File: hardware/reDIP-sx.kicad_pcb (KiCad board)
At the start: 6 copper layers, 17.8 x 40.6 mm, 134 parts, among them J1 DX07S016JA3, J10 Conn_01x01, J2 Conn_01x01, J3 Conn_01x01, J4 Conn_01x01, J5 Conn_01x06, J6 Conn_01x06, J7 Conn_01x10, J8 Conn_01x10, J9 Conn_01x01, Q1 PEMH4, Q2 PDTA143ZMB, U1 NCP163AFCT120T2G, U10 CBTD3306GT, U11 SN74CBTD16211DGVR, U2 NCP167AFCT330T2G, U3 FSA221UMX, U4 SGTL5000XNLA3, U5 ESP32-PICO-V3-02, U6 CP2102N-A02-GQFN24, U7 FSA8049UCX, U8 ICE40UP5K-SG48I, U9 APS6404L-3SQR-SN

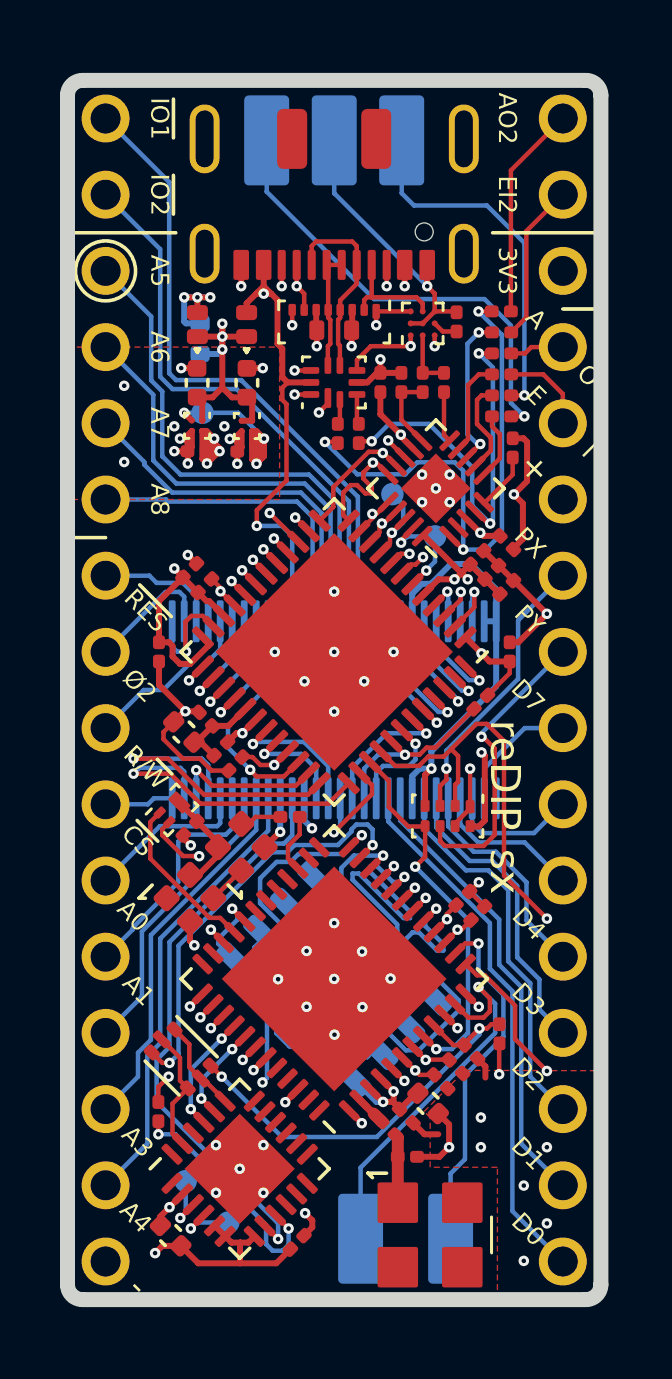
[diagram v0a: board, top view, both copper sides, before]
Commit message: Usability and manufacturability improvements
* Swapped pins for 3V3 and AO2
* Replaced 0.35mm pitch BGA LDOs with larger pitch parts, improved layout
* Removed IO2 pullup
* Added solder pad for RGB LED strip
* Increased solder mask clearance
* Updated silk screen
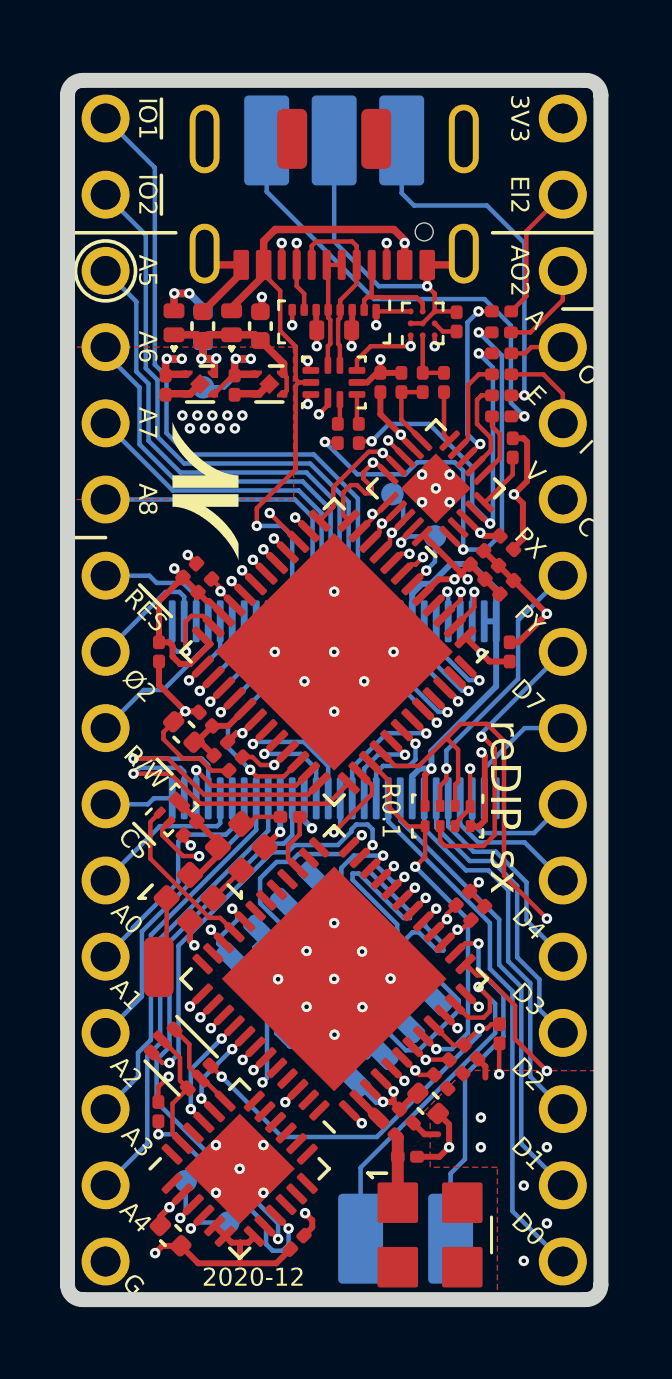
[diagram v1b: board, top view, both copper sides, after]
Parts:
- removed R12: 2.2k, Resistor_SMD:R_0201_0603Metric
- removed the SolderMask Opening D0.2mm at (105.3, 105.6)
- removed the SolderMask Opening D0.2mm at (104.1, 105.6)
- removed the SolderMask Opening D0.2mm at (103.6, 105.6)
- removed the SolderMask Opening D0.2mm at (102.5, 105.6)
- removed the SolderMask Opening D0.2mm at (105.0, 106.4)
- removed the SolderMask Opening D0.2mm at (102.3, 105.2)
- removed the SolderMask Opening D0.4mm at (105.3, 105.6)
- removed the SolderMask Opening D0.4mm at (102.7, 106.4)
- removed the SolderMask Opening D0.4mm at (102.3, 106.0)
- removed the SolderMask Opening D0.4mm at (102.3, 105.2)
- removed the SolderMask Opening D0.4mm at (104.1, 105.6)
- removed the SolderMask Opening D0.4mm at (103.6, 105.6)
- removed the SolderMask Opening D0.4mm at (102.5, 105.6)
- removed the SolderMask Opening D0.4mm at (103.8, 106.0)
- removed the SolderMask Opening D0.4mm at (104.0, 105.2)
- removed the SolderMask Opening D0.4mm at (105.0, 106.4)
- removed the SolderMask Opening D0.4mm at (104.4, 106.4)
- removed the SolderMask Opening D0.4mm at (103.4, 106.4)
- added J2: Conn_01x01, reDIP:SolderWirePad_1x01_SMD_1x2mm, F.Cu at (101.8, 123.2)
- added SolderMask Opening D0.2mm: SolderMask_Opening_D0.2mm, reDIP:SolderMask_Opening_D0.2mm, F.Cu at (103.3, 105.2)
- added SolderMask Opening D0.2mm: SolderMask_Opening_D0.2mm, reDIP:SolderMask_Opening_D0.2mm, F.Cu at (103.6, 104.8)
- added SolderMask Opening D0.2mm: SolderMask_Opening_D0.2mm, reDIP:SolderMask_Opening_D0.2mm, F.Cu at (103.1, 104.8)
- added SolderMask Opening D0.4mm: SolderMask_Opening_D0.4mm, reDIP:SolderMask_Opening_D0.4mm, B.Cu at (103.3, 105.2)
- added SolderMask Opening D0.4mm: SolderMask_Opening_D0.4mm, reDIP:SolderMask_Opening_D0.4mm, B.Cu at (103.6, 104.8)
- added SolderMask Opening D0.4mm: SolderMask_Opening_D0.4mm, reDIP:SolderMask_Opening_D0.4mm, B.Cu at (103.1, 104.8)
- added SolderMask Opening D0.4mm: SolderMask_Opening_D0.4mm, reDIP:SolderMask_Opening_D0.4mm, B.Cu at (104.1, 104.8)
- added SolderMask Opening D0.4mm: SolderMask_Opening_D0.4mm, reDIP:SolderMask_Opening_D0.4mm, B.Cu at (103.8, 105.2)
- added SolderMask Opening D0.4mm: SolderMask_Opening_D0.4mm, reDIP:SolderMask_Opening_D0.4mm, B.Cu at (104.3, 105.2)
- added SolderMask Opening D0.4mm: SolderMask_Opening_D0.4mm, reDIP:SolderMask_Opening_D0.4mm, B.Cu at (104.6, 104.8)
- added SolderMask Opening D0.4mm: SolderMask_Opening_D0.4mm, reDIP:SolderMask_Opening_D0.4mm, B.Cu at (102.6, 104.8)
- added SolderMask Opening D0.4mm: SolderMask_Opening_D0.4mm, reDIP:SolderMask_Opening_D0.4mm, B.Cu at (102.8, 105.2)
- added svg2mod: G***, reDIP:Nimrod-N, F.Cu at (103.3, 107.3)
- U1: value NCP163AFCT120T2G -> NCP163AMX120TBG; footprint ONSemi:WLCSP-4_0.64x0.64mm_Layout2x2_P0.35mm -> ONSemi:CASE711AJ_1.0x1.0mm_P0.65mm
- U2: value NCP167AFCT330T2G -> NCP167AMX330TBG; footprint ONSemi:WLCSP-4_0.64x0.64mm_Layout2x2_P0.35mm -> ONSemi:CASE711AJ_1.0x1.0mm_P0.65mm
- moved C4 2.44 mm to (102.0, 103.8), turned to 270 degrees
- moved C2 2.25 mm to (104.3, 103.8), turned to 270 degrees
- moved SolderMask Opening D0.2mm 1.99 mm to (104.6, 104.8)
- moved C1 1.94 mm to (105.2, 101.8)
- moved C3 1.90 mm to (103.2, 101.8)
- moved SolderMask Opening D0.2mm 1.61 mm to (102.6, 104.8)
- moved U1 1.59 mm to (105.5, 103.8), turned to 0 degrees
- moved U2 1.39 mm to (103.2, 103.8), turned to 0 degrees
- moved SolderMask Opening D0.2mm 1.22 mm to (104.1, 104.8)
- moved SolderMask Opening D0.2mm 1.18 mm to (104.3, 105.2)
- moved SolderMask Opening D0.2mm 0.92 mm to (102.8, 105.2)
- moved TP1 0.85 mm to (103.2, 103.9)
- moved D2 0.78 mm to (102.3, 101.7)
- moved C11 0.70 mm to (113.2, 101.3)
- moved C20 0.70 mm to (113.2, 102.0)
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- renumbered J9 to J10, J10 to J11, J2 to J3, J3 to J4, J4 to J5, J5 to J6, J6 to J7, J7 to J8, J8 to J9
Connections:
- D5 pad 1: (no net) -> /LED_DO
- J7 pad 1: /AUDIO_OUT_2 -> +3V3
- J7 pad 3: +3V3 -> /AUDIO_OUT_2
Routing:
- net +5V: track 45.5 -> 39.7 mm, vias 5 -> 4
- net +3V3: track 72.3 -> 66.9 mm, vias 22 -> 21
- net /AUDIO_OUT_2: track 7.15 -> 3.15 mm
- net VBUS: track 24.9 -> 28.3 mm, vias 4 -> 3
- net /D-: track 35.6 -> 32.5 mm
- net /ICE_~IO2~: track 6.12 -> 3.18 mm
- net /CC2: track 34.6 -> 37.5 mm
- net GND: track 64.9 -> 67.7 mm, vias 59 -> 57
- net /D+: track 36.1 -> 33.5 mm
- net /LED_DO: track 0.00 -> 2.40 mm
- net /A_SEL: track 53.6 -> 51.8 mm
- net /CC1: track 40.4 -> 42.2 mm
- net /Vcc: track 28.0 -> 26.5 mm, vias 3 -> 2
- net /~IO2~: track 19.0 -> 20.2 mm
- net /~IO1~: track 21.8 -> 22.9 mm
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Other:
- rule pad_to_mask_clearance: 0.025 -> 0.05
- board text added: "2020-12"
- board text added: "28"
- board text added: "A2"
- board text added: "C"
- board text added: "G"
- board text added: "L"
- board text added: "R"
- board text added: "R0.1"
- board text added: "V"
- board text removed: "+"
- board text removed: "-"
- board text removed: "27"
- board text removed: "4"
- board text removed: "5"
- board text removed: "LNL"
- board text removed: "LNR"

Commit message: A few small improvements
* Added SPI SCLK source termination for iCE40UP5K
* Changed R11 to 100Ω
* Changed C27 to 0.1µF
* Replaced a few capacitors with more readily available parts
* Added datasheet URLs for all parts
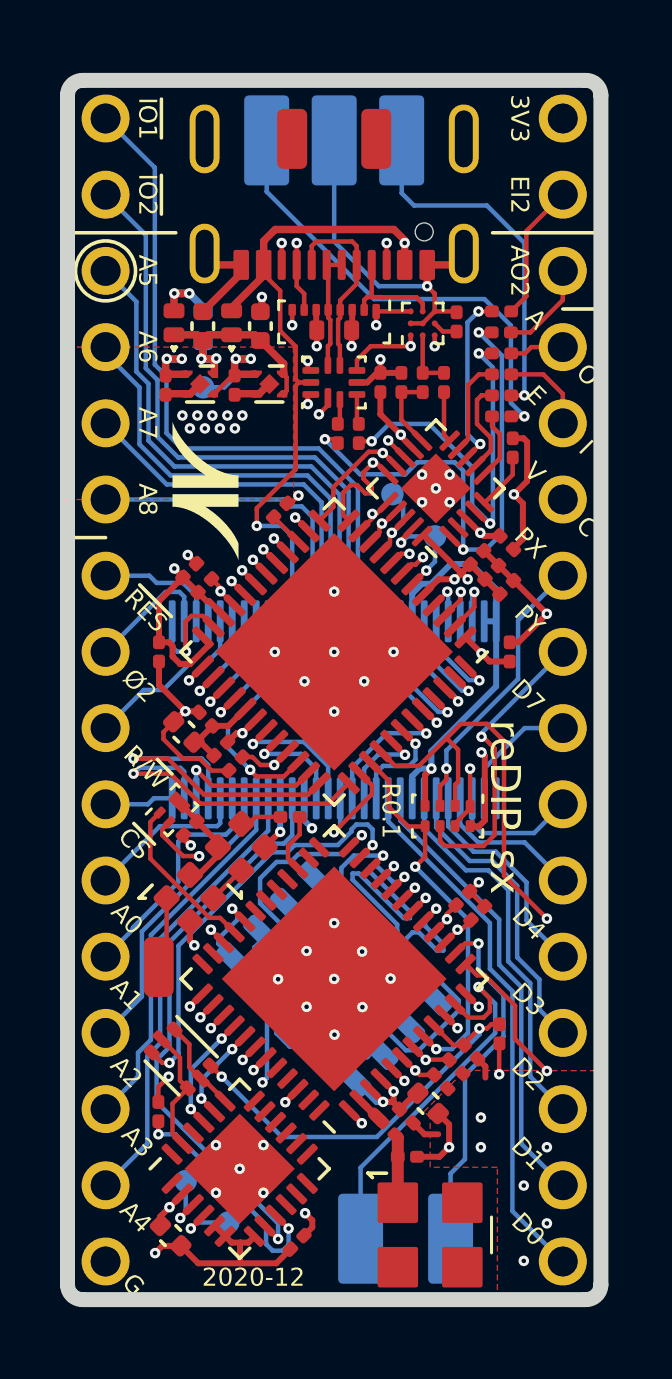
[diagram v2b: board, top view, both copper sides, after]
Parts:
- added R12: 22, Resistor_SMD:R_0201_0603Metric, F.Cu at (105.8, 108.0)
- C27: value 1uF -> 0.1uF
- R11: value 330 -> 100
- renumbered J3 to J2, J4 to J3, J5 to J4, J6 to J5, J7 to J6, J8 to J7, J9 to J8, J2 to J9
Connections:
- U8 pad 15: /SPI_SCLK -> Net-(R12-Pad1)
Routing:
- net /SPI_SCLK: track 32.4 -> 30.4 mm
- net Net-(R12-Pad1): track 0.00 -> 1.17 mm

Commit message: Usability and manufacturability improvements
* Increased minimum via size (good luck on increasing it further!)
* Corrected footprint rotation for D3 (IPC-7351)
* Removed split in stencil apertures for pin-in-paste
* Changed to shorter pin USB-C receptacle, yielding improved hole
  fill for partial pin penetration soldering
* Adjustments to fab and silk screen layers
* Added alternative ESP32 APLL configuration example to schematic
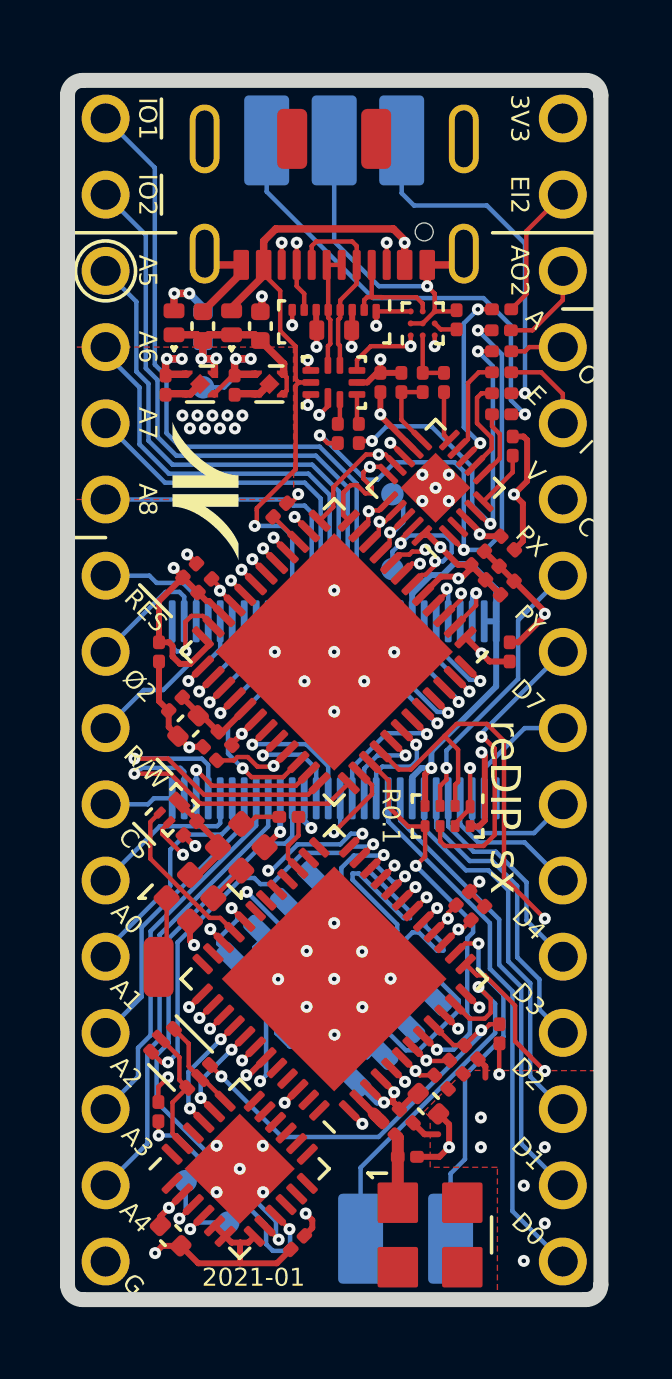
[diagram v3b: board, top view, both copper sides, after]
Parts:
- removed SolderMask Opening D0.4mm: SolderMask_Opening_D0.4mm, reDIP:SolderMask_Opening_D0.4mm (x9)
- added SolderMask D0.45mm: SolderMask_D0.45mm, reDIP:SolderMask_D0.45mm, B.Cu at (103.3, 105.2)
- added SolderMask D0.45mm: SolderMask_D0.45mm, reDIP:SolderMask_D0.45mm, B.Cu at (103.6, 104.8)
- added SolderMask D0.45mm: SolderMask_D0.45mm, reDIP:SolderMask_D0.45mm, B.Cu at (103.1, 104.8)
- added SolderMask D0.45mm: SolderMask_D0.45mm, reDIP:SolderMask_D0.45mm, B.Cu at (104.1, 104.8)
- added SolderMask D0.45mm: SolderMask_D0.45mm, reDIP:SolderMask_D0.45mm, B.Cu at (103.8, 105.2)
- added SolderMask D0.45mm: SolderMask_D0.45mm, reDIP:SolderMask_D0.45mm, B.Cu at (104.3, 105.2)
- added SolderMask D0.45mm: SolderMask_D0.45mm, reDIP:SolderMask_D0.45mm, B.Cu at (104.6, 104.8)
- added SolderMask D0.45mm: SolderMask_D0.45mm, reDIP:SolderMask_D0.45mm, B.Cu at (102.6, 104.8)
- added SolderMask D0.45mm: SolderMask_D0.45mm, reDIP:SolderMask_D0.45mm, B.Cu at (102.8, 105.2)
- J1: footprint JAE:USB_C_Receptacle_JAE_DX07S016JA3_PinInPaste -> JAE:USB_C_Receptacle_JAE_DX07S016JA1
- SolderMask D0.25mm: renamed from SolderMask Opening D0.2mm; value SolderMask_Opening_D0.2mm -> SolderMask_D0.25mm; footprint reDIP:SolderMask_Opening_D0.2mm -> reDIP:SolderMask_D0.25mm (x9)
- SolderMask D0.45mm: renamed from SolderMask Opening D0.4mm; value SolderMask_Opening_D0.4mm -> SolderMask_D0.45mm; footprint reDIP:SolderMask_Opening_D0.4mm -> reDIP:SolderMask_D0.45mm (x26)
- moved TP2 1.79 mm to (109.6, 109.9)
- moved C28 1.13 mm to (102.3, 114.4), turned to 225 degrees
- moved C31 0.92 mm to (103.5, 116.1), turned to 135 degrees
- moved R9 0.37 mm to (104.0, 115.6), turned to 135 degrees
- moved C29 0.24 mm to (102.8, 115.2), turned to 225 degrees
- moved C13 0.07 mm to (113.2, 103.4)
- moved C14 0.07 mm to (113.2, 104.1)
- moved C23 0.07 mm to (111.7, 101.6)
- moved C11 0.07 mm to (113.2, 101.3)
- moved C12 0.07 mm to (113.2, 104.8)
- moved C20 0.07 mm to (113.2, 102.0)
- moved C21 0.07 mm to (113.2, 102.7)
- moved C10 0.06 mm to (113.6, 105.8)
- turned D3 to 270 degrees
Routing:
- net GND: track 67.7 -> 65.2 mm
- net /I2S_WCLK: track 37.4 -> 39.6 mm
- net /I2C_SCL: track 20.0 -> 22.1 mm
- net /~CRESET~: track 18.4 -> 19.6 mm
- net /I2S_DOUT: track 35.3 -> 36.5 mm
- net /I2S_DIN: track 35.2 -> 36.4 mm
- net +3V3: track 66.9 -> 68.1 mm
- net +1V2: track 32.1 -> 33.2 mm
- net /D+: track 33.5 -> 32.5 mm
- net /I2S_BCLK: track 38.1 -> 38.9 mm
- net /SYS_CLK: track 35.3 -> 34.5 mm
- net Net-(C18-Pad2): track 18.1 -> 18.8 mm
- net /SPI_SIO0: track 32.9 -> 32.3 mm
- net /SPI_SIO2: track 32.6 -> 32.0 mm
- net /SPI_SIO3: track 32.4 -> 32.7 mm, vias 2 -> 4
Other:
- net class Default: via_dia 0.35 -> 0.4
- net class Power: via_dia 0.35 -> 0.4
- rule via_min_size: 0.35 -> 0.4
- board text added: "2021-01"
- board text added: "© 2021"
- board text removed: "2020-12"
- board text removed: "© 2020"
